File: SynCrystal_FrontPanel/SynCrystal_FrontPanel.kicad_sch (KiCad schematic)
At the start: 7 parts

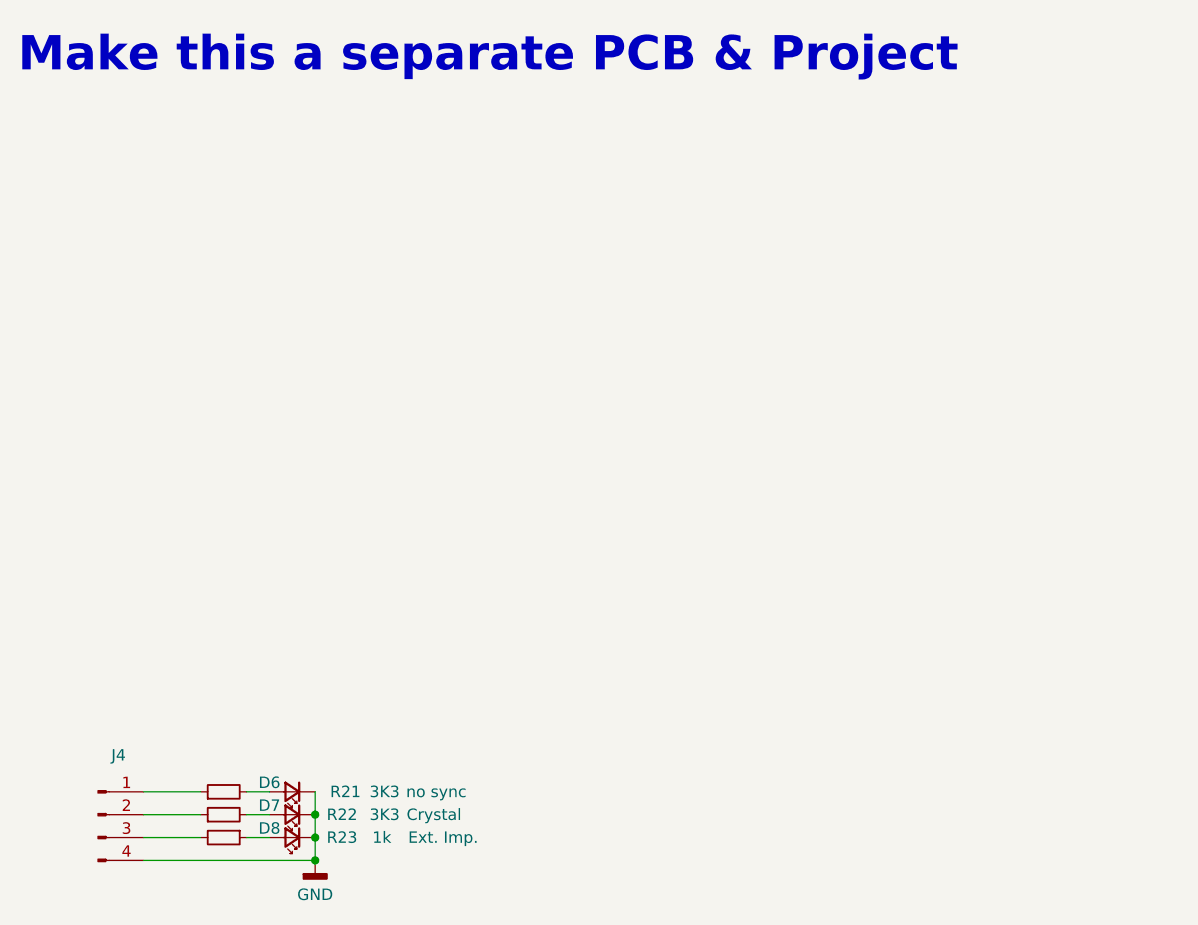
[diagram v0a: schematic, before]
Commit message: Starting to assign part numbers
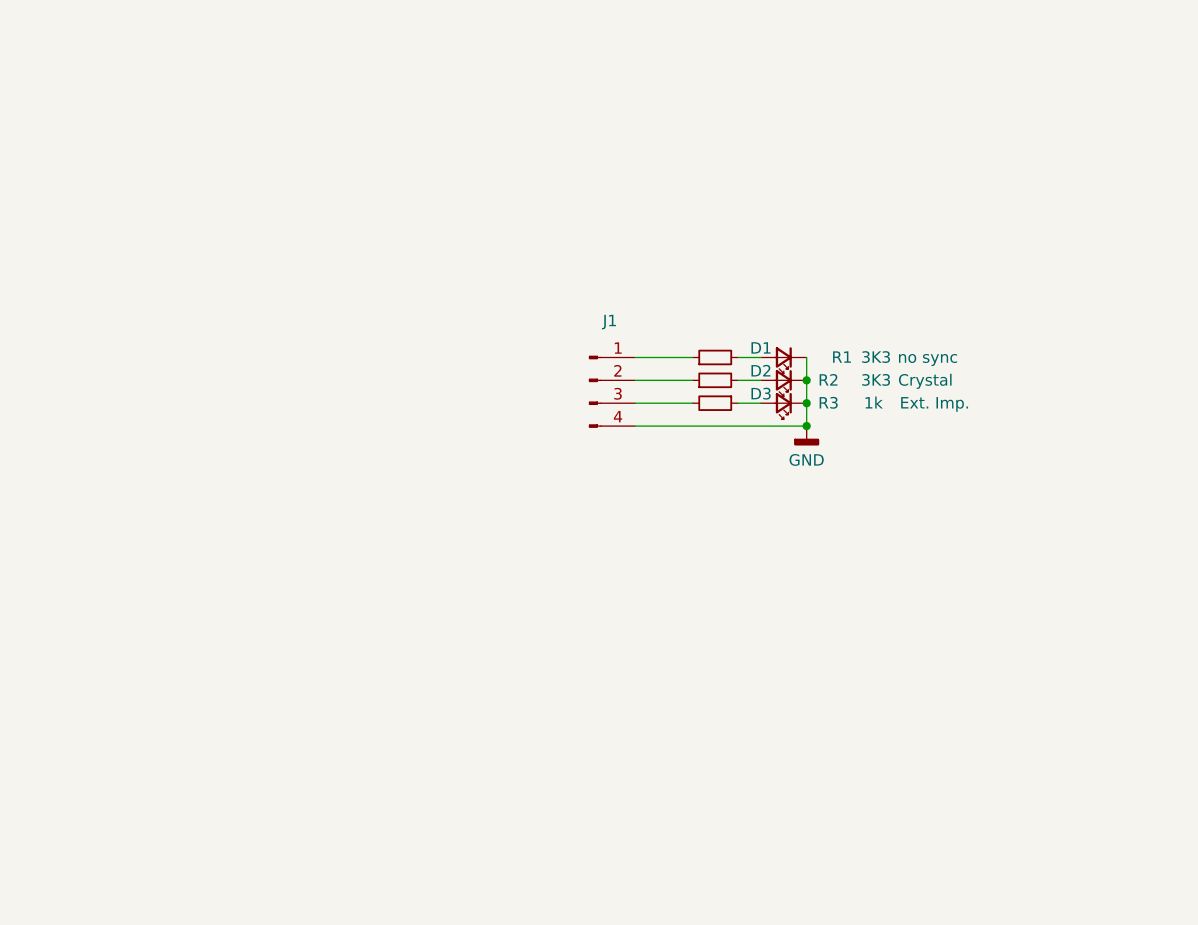
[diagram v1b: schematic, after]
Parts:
- removed D6: no sync, LED_SMD:LED_0805_2012Metric, symbol Device:LED_Small
- removed D7: Crystal, LED_SMD:LED_0805_2012Metric, symbol Device:LED_Small
- removed D8: Ext. Imp., LED_SMD:LED_0805_2012Metric, symbol Device:LED_Small
- removed J4: ~, easyEDA:HDR-SMD_HX-PM2.54-1X4P-TP-YQ, symbol Connector:Conn_01x04_Pin
- removed R21, R22: 3K3, Resistor_SMD:R_0603_1608Metric, symbol Device:R_Small
- removed R23: 1k, Resistor_SMD:R_0603_1608Metric, symbol Device:R_Small
- added D1: no sync, LED_SMD:LED_0805_2012Metric, symbol Device:LED_Small
- added D2: Crystal, LED_SMD:LED_0805_2012Metric, symbol Device:LED_Small
- added D3: Ext. Imp., LED_SMD:LED_0805_2012Metric, symbol Device:LED_Small
- added J1: ~, easyEDA:HDR-SMD_HX-PM2.54-1X4P-TP-YQ, symbol Connector:Conn_01x04_Pin
- added R1, R2: 3K3, Resistor_SMD:R_0603_1608Metric, symbol Device:R_Small
- added R3: 1k, Resistor_SMD:R_0603_1608Metric, symbol Device:R_Small
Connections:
- net GND: now also D1.1 (K), D2.1 (K), D3.1 (K), J1.4 (Pin_4)
- new net: J1.1 (Pin_1), R1.1
- new net: J1.2 (Pin_2), R2.1
- new net: J1.3 (Pin_3), R3.2
- new net: D2.2 (A), R2.2
- new net: D1.2 (A), R1.2
- new net: D3.2 (A), R3.1
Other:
- note removed: "Make this a separate PCB & Project"
